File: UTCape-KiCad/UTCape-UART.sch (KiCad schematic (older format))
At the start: 2 parts

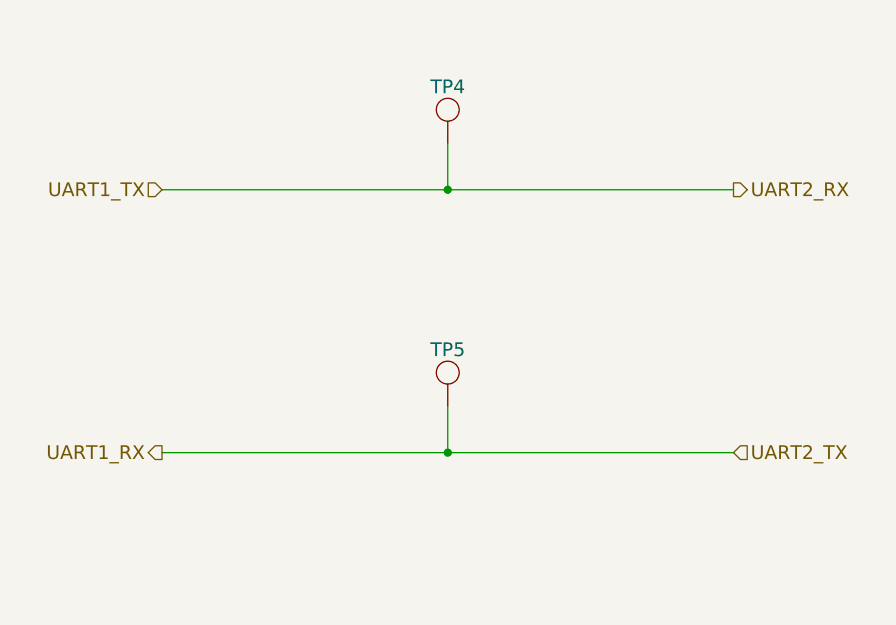
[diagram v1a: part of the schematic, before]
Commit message: added missing resistor in divider plus some protection resistors, regenerated fab files
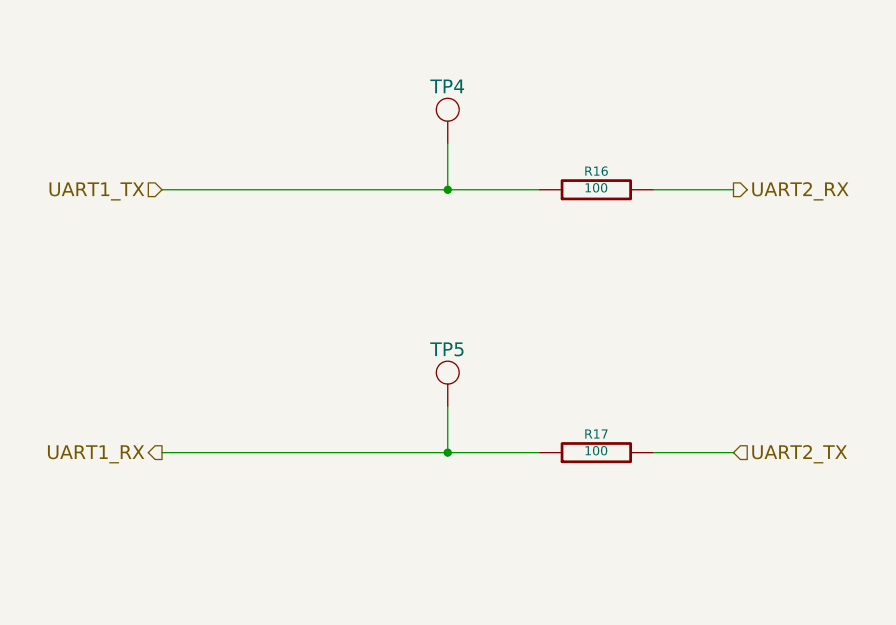
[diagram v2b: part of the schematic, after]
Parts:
- added R16, R17: 100, ~, symbol R
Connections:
- net UART1_RX: now also R17.1
- net UART1_TX: now also R16.1
- new net UART2_RX: R16.2
- new net UART2_TX: R17.2
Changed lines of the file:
@@
 Sheet 2 9
 Title ""
-Date "24 feb 2015"
+Date "24 mar 2015"
 Rev ""
 Comp ""
@@
 	6000 3150 6000 2950
 Connection ~ 6000 3150
-Wire Wire Line
-	4750 4300 7250 4300
-Wire Wire Line
-	4750 3150 7250 3150
 Text Notes 7350 7550 0    60   ~ 0
 UART Unit Test Wiring
@@
 03 43 83 61 8C 09 03 03 03 03 43 83 61 8C 09 03 03 03 03 43 83 61 8C 09 03 03 03 03 43 83 61 03
 60 D2 64 32 30 30 30 30 34 84 CF 1C 00 A9 00 9C 01 A8 8B 59 19 06 06 06 06 06 E9 E3 33 80 C5 FF
-07 47 25 A5 D2 E9 03 52 D8 00 00 00 00 49 45 4E 44 AE 42 60 82 4A $EndBitmap
+07 47 25 A5 D2 E9 03 52 D8 00 00 00 00 49 45 4E 44 AE 42 60 82 CF $EndBitmap
 EndData
 $EndBitmap
+Wire Wire Line
+	4750 3150 6400 3150
+Wire Wire Line
+	4750 4300 6400 4300
+$Comp
+L R R16
+U 1 1 54F697EB
+P 6650 3150
+F 0 "R16" V 6730 3150 40  0000 C CNN
+F 1 "100" V 6657 3151 40  0000 C CNN
+F 2 "~" V 6580 3150 30  0000 C CNN
+F 3 "~" H 6650 3150 30  0000 C CNN
+	1    6650 3150
+	0    -1   -1   0
+$EndComp
+$Comp
+L R R17
+U 1 1 54F697F8
+P 6650 4300
+F 0 "R17" V 6730 4300 40  0000 C CNN
+F 1 "100" V 6657 4301 40  0000 C CNN
+F 2 "~" V 6580 4300 30  0000 C CNN
+F 3 "~" H 6650 4300 30  0000 C CNN
+	1    6650 4300
+	0    -1   -1   0
+$EndComp
+Wire Wire Line
+	6900 3150 7250 3150
+Wire Wire Line
+	6900 4300 7250 4300
 $EndSCHEMATC
